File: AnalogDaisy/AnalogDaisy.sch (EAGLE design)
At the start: 53 parts, among them J1 POWERPOLE_POWER45A_DRILL, Q1 35A/25V/8.5mΩ, Q10 35A/25V/8.5mΩ, Q2 35A/25V/8.5mΩ, Q3 35A/25V/8.5mΩ, Q4 35A/25V/8.5mΩ, Q5 35A/25V/8.5mΩ, Q6 35A/25V/8.5mΩ, Q7 35A/25V/8.5mΩ, Q8 35A/25V/8.5mΩ, Q9 35A/25V/8.5mΩ

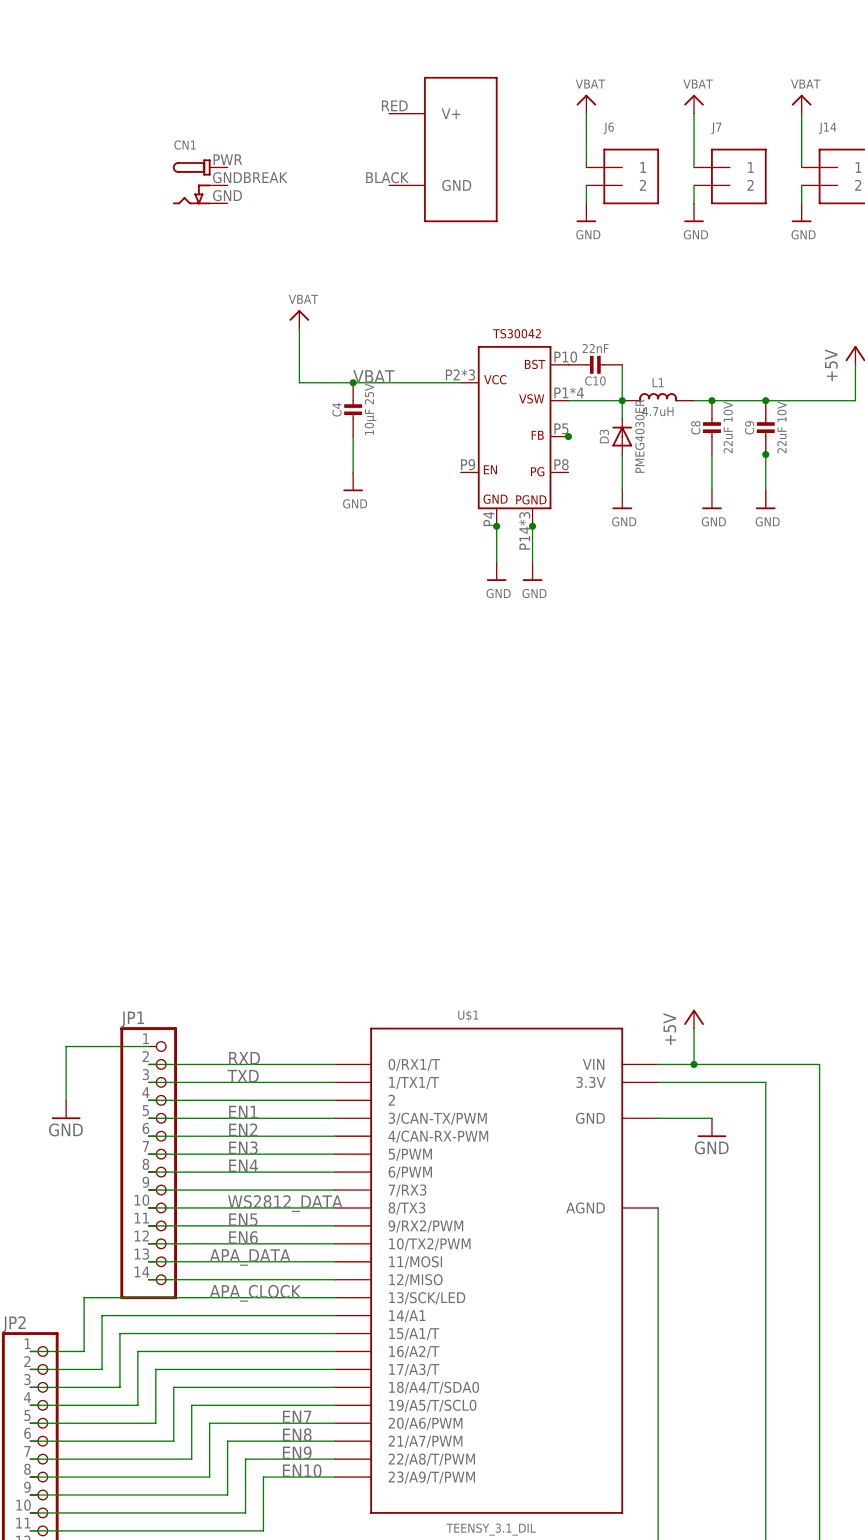
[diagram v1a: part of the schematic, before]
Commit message: Updated AnalogDaisy Wiring
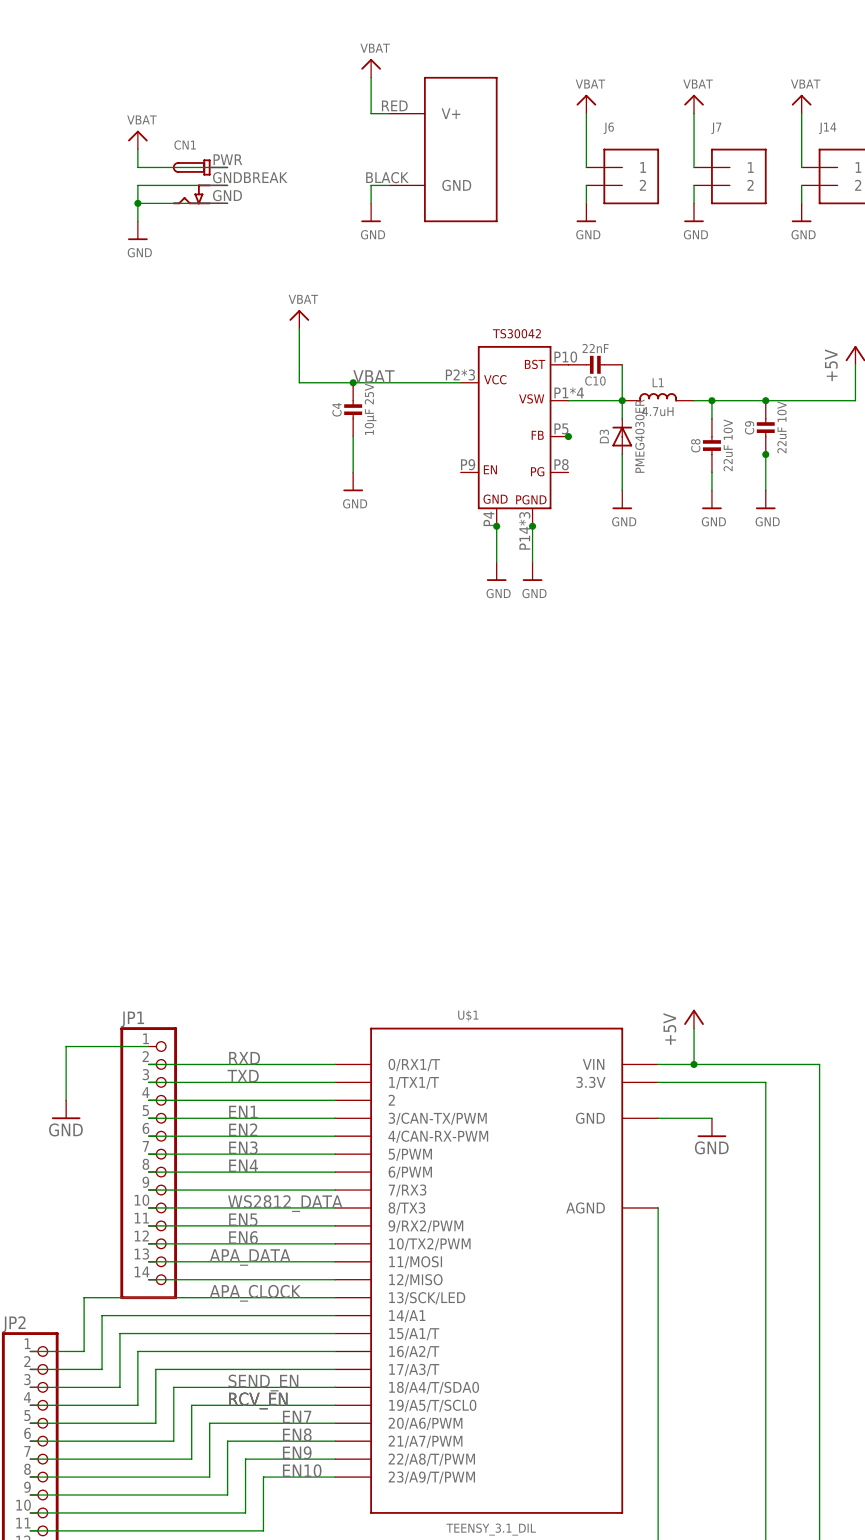
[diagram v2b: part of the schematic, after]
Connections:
- removed net N$16: JP2.6, U$1.18/A4/T/SDA0
- removed net N$17: JP2.7, U$1.19/A5/T/SCL0
- net +5V: now also C8.1
- net GND: now also CN1.GND, CN1.GNDBREAK, J1.GND
- net RCV_EN: now also JP2.7, U$1.19/A5/T/SCL0
- net SEND_EN: now also JP2.6, U$1.18/A4/T/SDA0
- net VBAT: now also CN1.PWR, J1.V+
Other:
- moved on the sheet: C8
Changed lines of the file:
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@@
 <part name="JP3" library="adafruit" deviceset="PINHD-1X3" device=""/>
 <part name="J15" library="My Connectors" deviceset="4PIN-JST/TE" device=""/>
-<part name="U$28" library="microbuilder" deviceset="VBAT" device=""/>
+<part name="VBAT" library="microbuilder" deviceset="VBAT" device=""/>
 <part name="U$29" library="microbuilder" deviceset="VBAT" device=""/>
 <part name="U$30" library="microbuilder" deviceset="VBAT" device=""/>
@@
 <part name="U$32" library="microbuilder" deviceset="GND" device=""/>
 <part name="U$33" library="microbuilder" deviceset="GND" device=""/>
+<part name="VBAT1" library="microbuilder" deviceset="VBAT" device=""/>
+<part name="VBAT2" library="microbuilder" deviceset="VBAT" device=""/>
+<part name="U$28" library="microbuilder" deviceset="GND" device=""/>
+<part name="U$34" library="microbuilder" deviceset="GND" device=""/>
 </parts>
 <sheets>
@@
 <instance part="U$2" gate="G$1" x="0" y="172.72"/>
 <instance part="C4" gate="G$1" x="-22.86" y="175.26"/>
-<instance part="C8" gate="G$1" x="27.94" y="172.72"/>
+<instance part="C8" gate="G$1" x="27.94" y="170.18"/>
 <instance part="C9" gate="G$1" x="35.56" y="172.72"/>
 <instance part="L1" gate="G$1" x="20.32" y="177.8"/>
@@
 <instance part="JP3" gate="A" x="-88.9" y="73.66"/>
 <instance part="J15" gate="G$1" x="-96.52" y="58.42" rot="R270"/>
-<instance part="U$28" gate="G$1" x="10.16" y="220.98"/>
+<instance part="VBAT" gate="G$1" x="10.16" y="220.98"/>
 <instance part="U$29" gate="G$1" x="25.4" y="220.98"/>
 <instance part="U$30" gate="G$1" x="40.64" y="220.98"/>
@@
 <instance part="U$32" gate="G$1" x="25.4" y="203.2"/>
 <instance part="U$33" gate="G$1" x="40.64" y="203.2"/>
+<instance part="VBAT1" gate="G$1" x="-20.32" y="226.06"/>
+<instance part="VBAT2" gate="G$1" x="-53.34" y="215.9"/>
+<instance part="U$28" gate="G$1" x="-20.32" y="203.2"/>
+<instance part="U$34" gate="G$1" x="-53.34" y="200.66"/>
 </instances>
 <busses>
@@
 <pinref part="C8" gate="G$1" pin="2"/>
 <pinref part="U$10" gate="G$1" pin="GND"/>
-<wire x1="27.94" y1="170.18" x2="27.94" y2="165.1" width="0.1524" layer="91"/>
+<wire x1="27.94" y1="167.64" x2="27.94" y2="165.1" width="0.1524" layer="91"/>
 </segment>
 <segment>
@@
 <pinref part="J14" gate="G$1" pin="2"/>
 <wire x1="40.64" y1="205.74" x2="40.64" y2="208.28" width="0.1524" layer="91"/>
+</segment>
+<segment>
+<pinref part="CN1" gate="G$1" pin="GND"/>
+<wire x1="-40.64" y1="205.74" x2="-53.34" y2="205.74" width="0.1524" layer="91"/>
+<pinref part="U$34" gate="G$1" pin="GND"/>
+<wire x1="-53.34" y1="205.74" x2="-53.34" y2="203.2" width="0.1524" layer="91"/>
+<pinref part="CN1" gate="G$1" pin="GNDBREAK"/>
+<wire x1="-40.64" y1="208.28" x2="-53.34" y2="208.28" width="0.1524" layer="91"/>
+<wire x1="-53.34" y1="208.28" x2="-53.34" y2="205.74" width="0.1524" layer="91"/>
+<junction x="-53.34" y="205.74"/>
+</segment>
+<segment>
+<pinref part="J1" gate="G$1" pin="GND"/>
+<wire x1="-17.78" y1="208.28" x2="-20.32" y2="208.28" width="0.1524" layer="91"/>
+<pinref part="U$28" gate="G$1" pin="GND"/>
+<wire x1="-20.32" y1="208.28" x2="-20.32" y2="205.74" width="0.1524" layer="91"/>
 </segment>
 </net>
@@
 </segment>
 <segment>
-<pinref part="U$28" gate="G$1" pin="VBAT"/>
+<pinref part="VBAT" gate="G$1" pin="VBAT"/>
 <wire x1="10.16" y1="210.82" x2="10.16" y2="218.44" width="0.1524" layer="91"/>
 </segment>
@@
 <pinref part="U$30" gate="G$1" pin="VBAT"/>
 <wire x1="40.64" y1="210.82" x2="40.64" y2="218.44" width="0.1524" layer="91"/>
+</segment>
+<segment>
+<pinref part="VBAT2" gate="G$1" pin="VBAT"/>
+<wire x1="-53.34" y1="213.36" x2="-53.34" y2="210.82" width="0.1524" layer="91"/>
+<pinref part="CN1" gate="G$1" pin="PWR"/>
+<wire x1="-53.34" y1="210.82" x2="-40.64" y2="210.82" width="0.1524" layer="91"/>
+</segment>
+<segment>
+<pinref part="J1" gate="G$1" pin="V+"/>
+<wire x1="-17.78" y1="218.44" x2="-20.32" y2="218.44" width="0.1524" layer="91"/>
+<pinref part="VBAT1" gate="G$1" pin="VBAT"/>
+<wire x1="-20.32" y1="218.44" x2="-20.32" y2="223.52" width="0.1524" layer="91"/>
 </segment>
 </net>
@@
 <wire x1="99.06" y1="165.1" x2="83.82" y2="165.1" width="0.1524" layer="91"/>
 <label x="83.82" y="165.1" size="1.778" layer="95"/>
+</segment>
+<segment>
+<pinref part="U$1" gate="G$1" pin="19/A5/T/SCL0"/>
+<wire x1="-25.4" y1="35.56" x2="-45.72" y2="35.56" width="0.1524" layer="91"/>
+<wire x1="-45.72" y1="35.56" x2="-45.72" y2="27.94" width="0.1524" layer="91"/>
+<pinref part="JP2" gate="A" pin="7"/>
+<wire x1="-45.72" y1="27.94" x2="-68.58" y2="27.94" width="0.1524" layer="91"/>
+<label x="-40.64" y="35.56" size="1.778" layer="95"/>
+<label x="-40.64" y="35.56" size="1.778" layer="95"/>
 </segment>
 </net>
@@
 <label x="83.82" y="167.64" size="1.778" layer="95"/>
 </segment>
+<segment>
+<pinref part="U$1" gate="G$1" pin="18/A4/T/SDA0"/>
+<wire x1="-25.4" y1="38.1" x2="-48.26" y2="38.1" width="0.1524" layer="91"/>
+<wire x1="-48.26" y1="38.1" x2="-48.26" y2="30.48" width="0.1524" layer="91"/>
+<pinref part="JP2" gate="A" pin="6"/>
+<wire x1="-48.26" y1="30.48" x2="-68.58" y2="30.48" width="0.1524" layer="91"/>
+<label x="-40.64" y="38.1" size="1.778" layer="95"/>
+</segment>
 </net>
 <net name="N$2" class="0">
@@
 <pinref part="P+3" gate="1" pin="+5V"/>
 <wire x1="48.26" y1="177.8" x2="48.26" y2="182.88" width="0.1524" layer="91"/>
+<pinref part="C8" gate="G$1" pin="1"/>
+<wire x1="27.94" y1="175.26" x2="27.94" y2="177.8" width="0.1524" layer="91"/>
 </segment>
 <segment>
@@
 </segment>
 </net>
-<net name="N$16" class="0">
-<segment>
-<pinref part="U$1" gate="G$1" pin="18/A4/T/SDA0"/>
-<wire x1="-25.4" y1="38.1" x2="-48.26" y2="38.1" width="0.1524" layer="91"/>
-<wire x1="-48.26" y1="38.1" x2="-48.26" y2="30.48" width="0.1524" layer="91"/>
-<pinref part="JP2" gate="A" pin="6"/>
-<wire x1="-48.26" y1="30.48" x2="-68.58" y2="30.48" width="0.1524" layer="91"/>
-</segment>
-</net>
-<net name="N$17" class="0">
-<segment>
-<pinref part="U$1" gate="G$1" pin="19/A5/T/SCL0"/>
-<wire x1="-25.4" y1="35.56" x2="-45.72" y2="35.56" width="0.1524" layer="91"/>
-<wire x1="-45.72" y1="35.56" x2="-45.72" y2="27.94" width="0.1524" layer="91"/>
-<pinref part="JP2" gate="A" pin="7"/>
-<wire x1="-45.72" y1="27.94" x2="-68.58" y2="27.94" width="0.1524" layer="91"/>
-</segment>
-</net>
